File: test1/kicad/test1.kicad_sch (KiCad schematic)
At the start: 0 parts

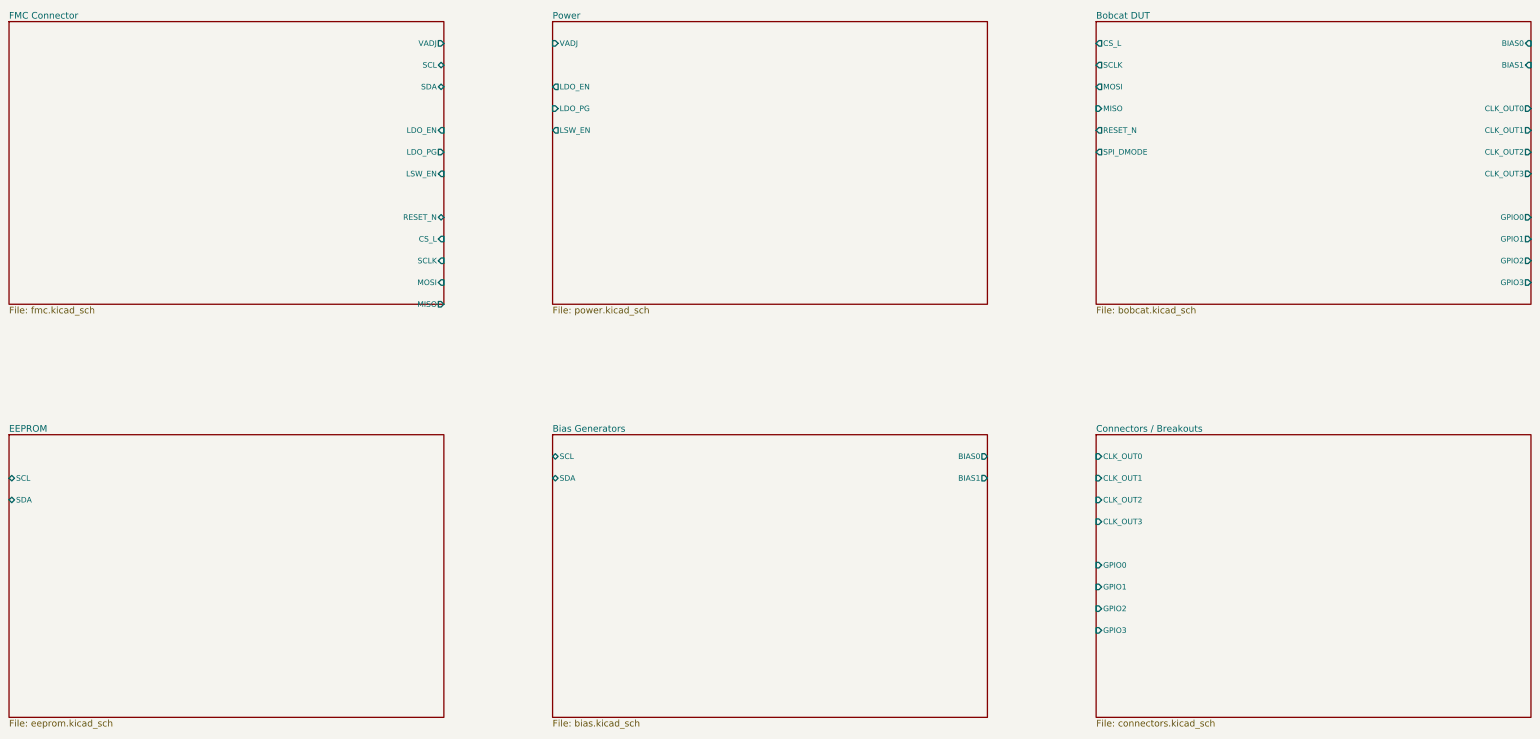
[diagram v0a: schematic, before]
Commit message: Project-wide connectivity audit: refdes uniqueness + hier-label correctness
Added test1/verify_project.py as a kicad-cli-erc substitute (the dev
build doesn't ship _cvpcb.kiface, so sch erc is broken). The verifier
parses all .kicad_sch files and checks:
  1. Duplicate refdes (KiCad's refdes namespace is project-wide).
  2. Parent sheet-pin name + direction matches child hierarchical_label.
  3. Orphan child hierarchical_labels (no matching parent pin).

First run flagged 48 issues. Now reports 0.

Refdes scheme — per-sheet decade ranges so global namespace stays unique:
  FMC 1-9 (J1-J4)
  Power 10-19 (U10/U11, R10/R11, C10-C16, J10-J12)
  Bobcat 20-29 (U20, R20/R21, C20-C25)
  EEPROM 30-39 (U30, R30/R31, C30)
  Bias 40-49 (U40/U41 [U41 dual-unit OPA], Q40-Q43, R40/R41, C40-C43)
  Connectors 50-59 (J50-J57, TP50-TP52)

Hierarchical / global label rework:
  - Parent sheet-pin directions corrected to match child labels (was
    flipped on every Bobcat SPI pin and on FMC's LDO_EN/LSW_EN/LDO_PG).
  - Bobcat SPI labels: passive → input/output as appropriate.
  - Project-wide nets converted to global_label (auto-tie by name, no
    parent pins): SCL, SDA, SAMPLE_OUT*, OSC_EN, WEIGHT_EN, SAMPLE_TRIG,
    BIAS_ISO0/1, CS_L, SCLK, MOSI, MISO, SPI_DMODE, RESET_N.
  - hier_label retained for clean 2-sheet pairs: VADJ, LDO_EN, LDO_PG,
    LSW_EN (FMC ↔ Power); BIAS0/1 (Bias ↔ Bobcat); CLK_OUT0-3, GPIO0-3
    (Bobcat ↔ Connectors).
  - Visual cue in renders: globals render as boxed rectangles; hierarchical
    labels render as arrows — handy when scanning a sheet.

Memory: appended five connectivity-correctness lessons to
feedback_kicad_generator_lessons.md (refdes namespace, parent/child
direction parity, no-passive-for-real-signals, global vs hier decision
table, verify-after-every-change).

Co-Authored-By: Claude Opus 4.7 (1M context) <noreply@anthropic.com>
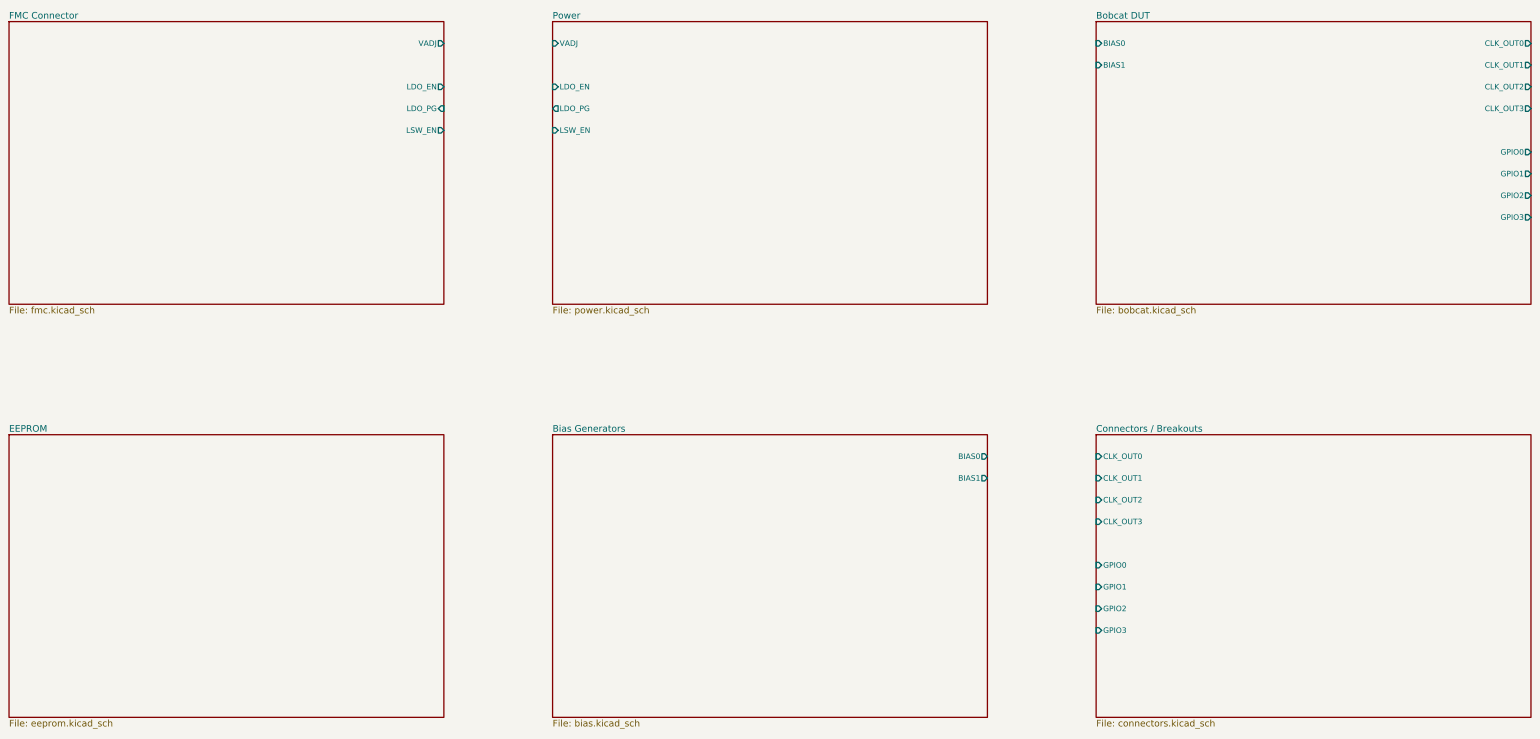
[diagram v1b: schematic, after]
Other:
- sheet Bias Generators ports: added none; removed SCL, SDA
- sheet Bobcat DUT ports: added none; removed CS_L, MISO, MOSI, RESET_N, SCLK, SPI_DMODE
- sheet EEPROM ports: added none; removed SCL, SDA
- sheet FMC Connector ports: added none; removed CS_L, MISO, MOSI, RESET_N, SCL, SCLK, SDA
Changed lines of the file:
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@@
       (effects (font (size 1.524 1.524)) (justify left top)))
     (pin "VADJ" output (at 130 40 0) (effects (font (size 1.27 1.27)) (justify right)))
-    (pin "SCL" bidirectional (at 130 45 0) (effects (font (size 1.27 1.27)) (justify right)))
-    (pin "SDA" bidirectional (at 130 50 0) (effects (font (size 1.27 1.27)) (justify right)))
-    (pin "LDO_EN" input (at 130 60 0) (effects (font (size 1.27 1.27)) (justify right)))
-    (pin "LDO_PG" output (at 130 65 0) (effects (font (size 1.27 1.27)) (justify right)))
-    (pin "LSW_EN" input (at 130 70 0) (effects (font (size 1.27 1.27)) (justify right)))
-    (pin "RESET_N" bidirectional (at 130 80 0) (effects (font (size 1.27 1.27)) (justify right)))
-    (pin "CS_L" input (at 130 85 0) (effects (font (size 1.27 1.27)) (justify right)))
-    (pin "SCLK" input (at 130 90 0) (effects (font (size 1.27 1.27)) (justify right)))
-    (pin "MOSI" input (at 130 95 0) (effects (font (size 1.27 1.27)) (justify right)))
-    (pin "MISO" output (at 130 100 0) (effects (font (size 1.27 1.27)) (justify right)))
+    (pin "LDO_EN" output (at 130 50 0) (effects (font (size 1.27 1.27)) (justify right)))
+    (pin "LDO_PG" input (at 130 55 0) (effects (font (size 1.27 1.27)) (justify right)))
+    (pin "LSW_EN" output (at 130 60 0) (effects (font (size 1.27 1.27)) (justify right)))
     (instances (project "test1" (path "/4ed7a046-ef33-57d9-8730-321c05965af3" (page "2"))))
   )
@@
       (effects (font (size 1.524 1.524)) (justify left top)))
     (pin "VADJ" input (at 155 40 180) (effects (font (size 1.27 1.27)) (justify left)))
-    (pin "LDO_EN" output (at 155 50 180) (effects (font (size 1.27 1.27)) (justify left)))
-    (pin "LDO_PG" input (at 155 55 180) (effects (font (size 1.27 1.27)) (justify left)))
-    (pin "LSW_EN" output (at 155 60 180) (effects (font (size 1.27 1.27)) (justify left)))
+    (pin "LDO_EN" input (at 155 50 180) (effects (font (size 1.27 1.27)) (justify left)))
+    (pin "LDO_PG" output (at 155 55 180) (effects (font (size 1.27 1.27)) (justify left)))
+    (pin "LSW_EN" input (at 155 60 180) (effects (font (size 1.27 1.27)) (justify left)))
     (instances (project "test1" (path "/4ed7a046-ef33-57d9-8730-321c05965af3" (page "3"))))
   )
@@
     (property "Sheetfile" "bobcat.kicad_sch" (at 280 100.5 0)
       (effects (font (size 1.524 1.524)) (justify left top)))
-    (pin "CS_L" output (at 280 40 180) (effects (font (size 1.27 1.27)) (justify left)))
-    (pin "SCLK" output (at 280 45 180) (effects (font (size 1.27 1.27)) (justify left)))
-    (pin "MOSI" output (at 280 50 180) (effects (font (size 1.27 1.27)) (justify left)))
-    (pin "MISO" input (at 280 55 180) (effects (font (size 1.27 1.27)) (justify left)))
-    (pin "RESET_N" output (at 280 60 180) (effects (font (size 1.27 1.27)) (justify left)))
-    (pin "SPI_DMODE" output (at 280 65 180) (effects (font (size 1.27 1.27)) (justify left)))
-    (pin "BIAS0" input (at 380 40 0) (effects (font (size 1.27 1.27)) (justify right)))
-    (pin "BIAS1" input (at 380 45 0) (effects (font (size 1.27 1.27)) (justify right)))
-    (pin "CLK_OUT0" output (at 380 55 0) (effects (font (size 1.27 1.27)) (justify right)))
-    (pin "CLK_OUT1" output (at 380 60 0) (effects (font (size 1.27 1.27)) (justify right)))
-    (pin "CLK_OUT2" output (at 380 65 0) (effects (font (size 1.27 1.27)) (justify right)))
-    (pin "CLK_OUT3" output (at 380 70 0) (effects (font (size 1.27 1.27)) (justify right)))
-    (pin "GPIO0" output (at 380 80 0) (effects (font (size 1.27 1.27)) (justify right)))
-    (pin "GPIO1" output (at 380 85 0) (effects (font (size 1.27 1.27)) (justify right)))
-    (pin "GPIO2" output (at 380 90 0) (effects (font (size 1.27 1.27)) (justify right)))
-    (pin "GPIO3" output (at 380 95 0) (effects (font (size 1.27 1.27)) (justify right)))
+    (pin "BIAS0" input (at 280 40 180) (effects (font (size 1.27 1.27)) (justify left)))
+    (pin "BIAS1" input (at 280 45 180) (effects (font (size 1.27 1.27)) (justify left)))
+    (pin "CLK_OUT0" output (at 380 40 0) (effects (font (size 1.27 1.27)) (justify right)))
+    (pin "CLK_OUT1" output (at 380 45 0) (effects (font (size 1.27 1.27)) (justify right)))
+    (pin "CLK_OUT2" output (at 380 50 0) (effects (font (size 1.27 1.27)) (justify right)))
+    (pin "CLK_OUT3" output (at 380 55 0) (effects (font (size 1.27 1.27)) (justify right)))
+    (pin "GPIO0" output (at 380 65 0) (effects (font (size 1.27 1.27)) (justify right)))
+    (pin "GPIO1" output (at 380 70 0) (effects (font (size 1.27 1.27)) (justify right)))
+    (pin "GPIO2" output (at 380 75 0) (effects (font (size 1.27 1.27)) (justify right)))
+    (pin "GPIO3" output (at 380 80 0) (effects (font (size 1.27 1.27)) (justify right)))
     (instances (project "test1" (path "/4ed7a046-ef33-57d9-8730-321c05965af3" (page "4"))))
   )
@@
     (property "Sheetfile" "eeprom.kicad_sch" (at 30 195.5 0)
       (effects (font (size 1.524 1.524)) (justify left top)))
-    (pin "SCL" bidirectional (at 30 140 180) (effects (font (size 1.27 1.27)) (justify left)))
-    (pin "SDA" bidirectional (at 30 145 180) (effects (font (size 1.27 1.27)) (justify left)))
     (instances (project "test1" (path "/4ed7a046-ef33-57d9-8730-321c05965af3" (page "5"))))
   )
@@
     (property "Sheetfile" "bias.kicad_sch" (at 155 195.5 0)
       (effects (font (size 1.524 1.524)) (justify left top)))
-    (pin "SCL" bidirectional (at 155 135 180) (effects (font (size 1.27 1.27)) (justify left)))
-    (pin "SDA" bidirectional (at 155 140 180) (effects (font (size 1.27 1.27)) (justify left)))
     (pin "BIAS0" output (at 255 135 0) (effects (font (size 1.27 1.27)) (justify right)))
     (pin "BIAS1" output (at 255 140 0) (effects (font (size 1.27 1.27)) (justify right)))
